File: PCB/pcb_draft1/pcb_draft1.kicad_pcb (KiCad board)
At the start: 2 copper layers, 100 x 100 mm, 83 parts, among them J1 RollerServos, J2 12V_Power A97996-ND, J3 HomeSwitch, J4 Therm1, J5 ArdAnalogTherm, J6 Therm2, J7 Conn_02x02_Odd_Even, Q1 DMN6140L, Q10 DMN6140L, Q11 DMN6140L, Q12 DMN6140L, Q13 DMN6140L, Q14 DMN6140L, Q15 DMN6140L, Q2 DMN6140L, Q3 DMN6140L, Q4 DMN6140L, Q5 DMN6140L, Q6 DMN6140L, Q7 DMN6140L, Q8 DMN6140L, Q9 DMN6140L, U1 STSPIN820, U2 STSPIN820, U3 AMS1117-5.0 RasPi, U4 AMS1117-5.0 Servo, Y1 Arduino_Mega_Bottom_Pins1

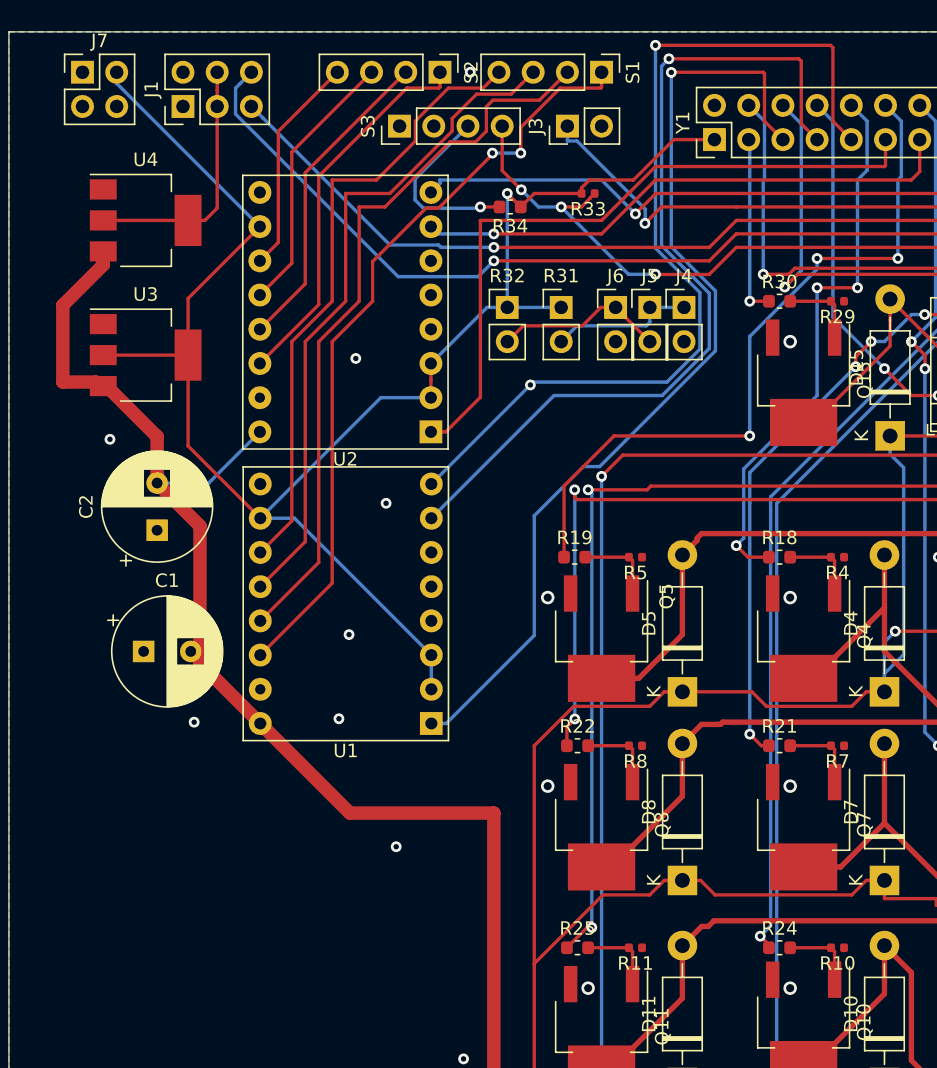
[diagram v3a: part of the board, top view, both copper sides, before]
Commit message: fix few unconnected pads
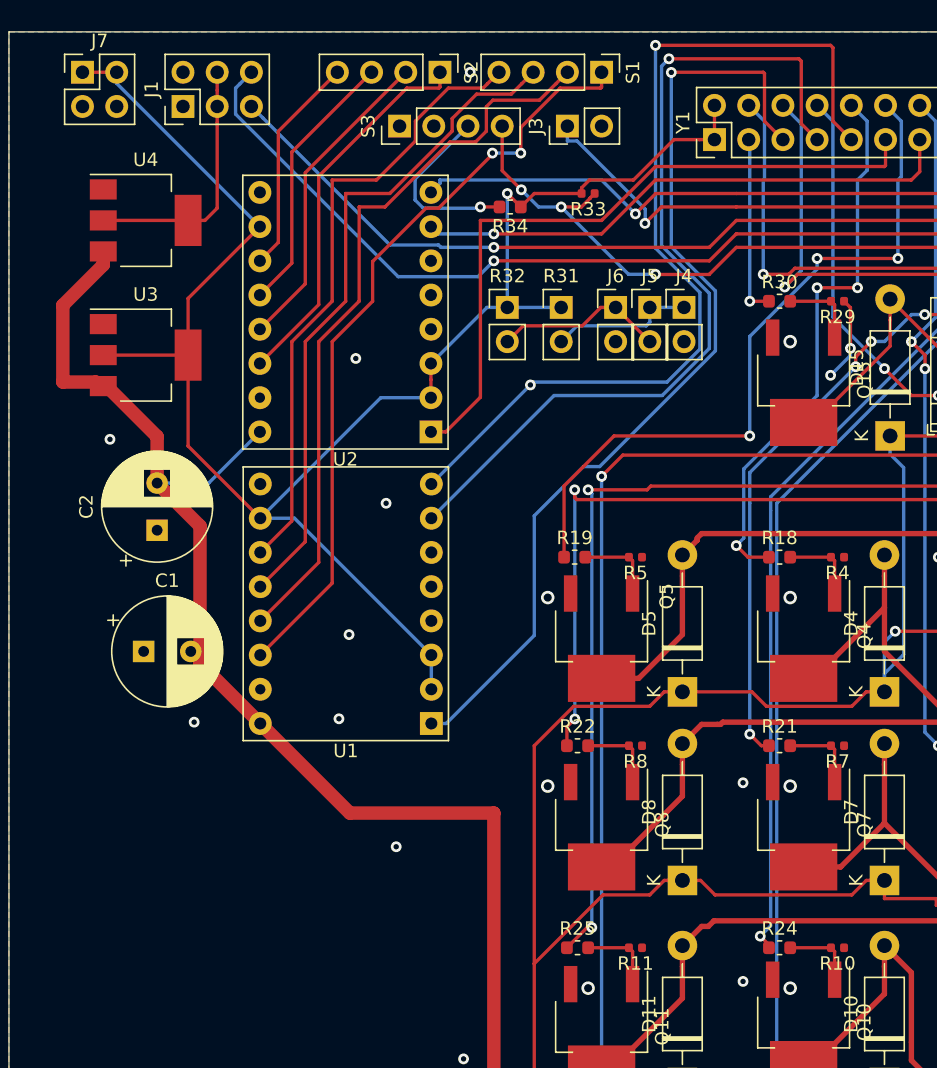
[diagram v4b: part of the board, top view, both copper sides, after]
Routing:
- net GND: track 3.00 -> 9.31 mm, vias 27 -> 31
- net 5V: track 124.6 -> 129.7 mm
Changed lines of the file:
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@@
     (thickness 1.6)
     (drawings 4)
-    (tracks 837)
+    (tracks 847)
     (zones 0)
     (modules 83)
@@
   (page A4)
   (layers
-    (0 F.Cu signal)
+    (0 F.Cu signal hide)
     (31 B.Cu signal)
     (32 B.Adhes user hide)
@@
   (via (at 50.75 39.25) (size 0.8) (drill 0.4) (layers F.Cu B.Cu) (net 2))
   (via (at 59.25 18) (size 0.8) (drill 0.4) (layers F.Cu B.Cu) (net 2))
+  (via (at 79.5 70.75) (size 0.8) (drill 0.4) (layers F.Cu B.Cu) (net 2))
+  (via (at 79.5 85.5) (size 0.8) (drill 0.4) (layers F.Cu B.Cu) (net 2))
+  (via (at 87.474694 38.5) (size 0.8) (drill 0.4) (layers F.Cu B.Cu) (net 2))
+  (segment (start 87 35) (end 87.474694 35.474694) (width 0.25) (layer F.Cu) (net 2))
+  (segment (start 87.474694 35.474694) (end 87.474694 38.5) (width 0.25) (layer F.Cu) (net 2))
+  (via (at 86 40.5) (size 0.8) (drill 0.4) (layers F.Cu B.Cu) (net 2))
+  (segment (start 87.474694 39.025306) (end 86 40.5) (width 0.25) (layer B.Cu) (net 2))
+  (segment (start 87.474694 38.5) (end 87.474694 39.025306) (width 0.25) (layer B.Cu) (net 2))
   (segment (start 64 27) (end 63 28) (width 0.25) (layer F.Cu) (net 3))
   (segment (start 67.515 27) (end 64 27) (width 0.25) (layer F.Cu) (net 3))
@@
   (segment (start 43.66 51.11) (end 46.2 51.11) (width 0.25) (layer B.Cu) (net 3))
   (segment (start 56.36 61.27) (end 56.36 63.81) (width 0.25) (layer B.Cu) (net 3))
+  (segment (start 33 18) (end 30.46 18) (width 0.25) (layer F.Cu) (net 3))
+  (segment (start 77.38 23) (end 77.38 20.46) (width 0.25) (layer F.Cu) (net 3))
   (segment (start 118 36.395634) (end 118 34.84) (width 0.4) (layer F.Cu) (net 4))
   (segment (start 118 38.9) (end 118 36.395634) (width 0.4) (layer F.Cu) (net 4))
